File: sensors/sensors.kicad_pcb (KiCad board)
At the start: 2 copper layers, 20 x 50 mm, 6 parts, among them J1 Conn 1x3, U1 TCRT5000

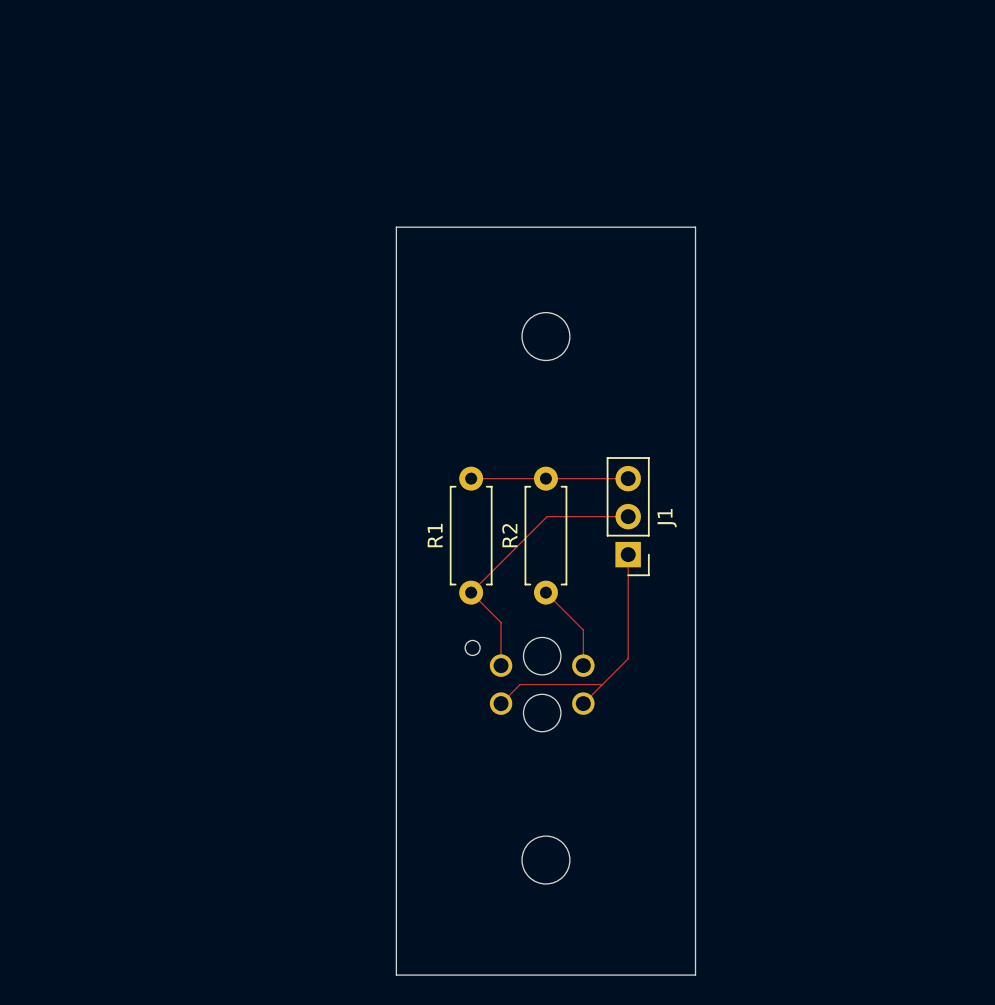
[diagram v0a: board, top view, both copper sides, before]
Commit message: Added a potentiometer to the sensor board.
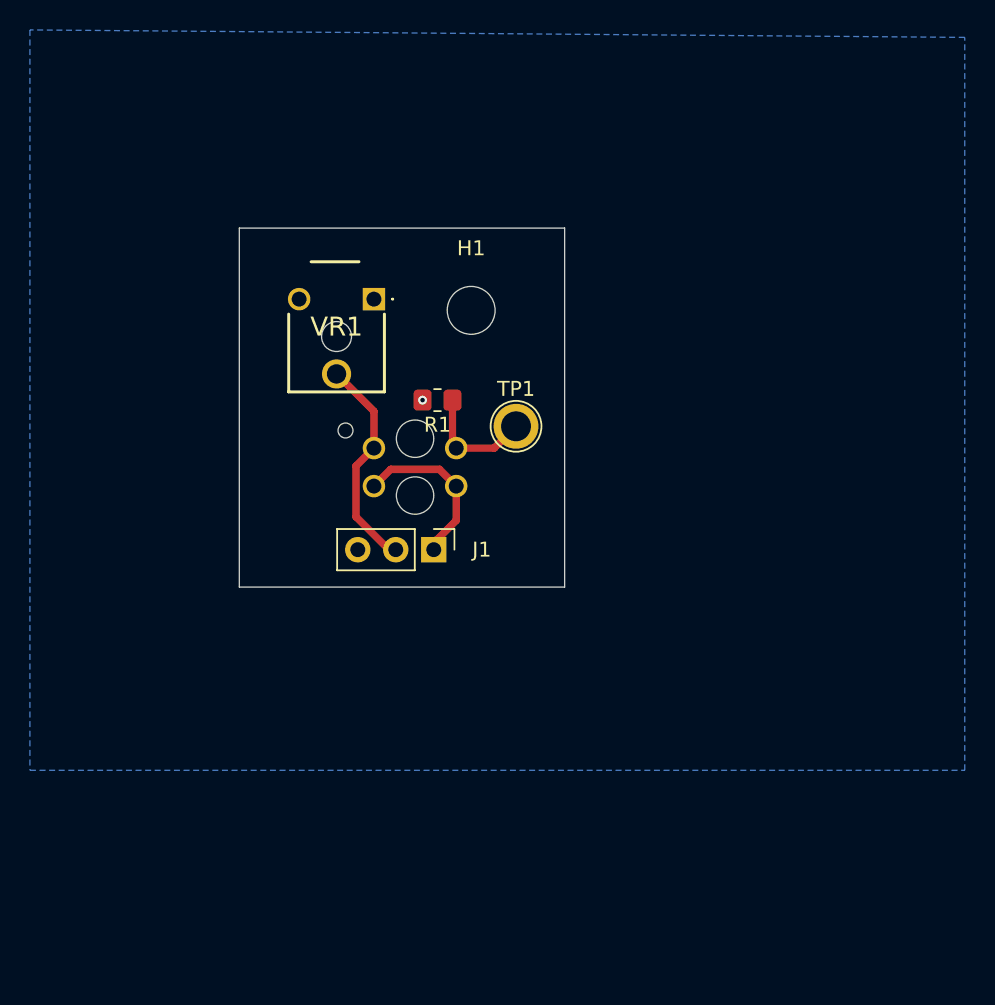
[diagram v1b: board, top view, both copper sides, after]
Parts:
- removed H2: MountingHole, MountingHole:MountingHole_3.2mm_M3
- removed R2: 2k, Resistor_THT:R_Axial_DIN0207_L6.3mm_D2.5mm_P7.62mm_Horizontal
- added TP1: Cathode, TestPoint:TestPoint_Plated_Hole_D2.0mm, F.Cu at (158.5, 75.5)
- added VR1: N6L50T0C-102-3030, N6L50T0C-103-3030:N6L50T0C1033030, F.Cu at (149.0, 67.0)
- R1: value 50R -> 2k2; footprint Resistor_THT:R_Axial_DIN0207_L6.3mm_D2.5mm_P7.62mm_Horizontal -> Resistor_SMD:R_0805_2012Metric_Pad1.20x1.40mm_HandSolder
- moved U1 16.8 mm to (151.8, 78.2)
- moved R1 13.1 mm to (153.2, 73.8), turned to 180 degrees
- moved J1 13.0 mm to (153.0, 83.8), turned to -90 degrees
- moved H1 5.30 mm to (155.5, 67.8)
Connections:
- net Vss renamed Vcc
- R1 pad 1: Vout -> Net-(R1-Pad1)
- U1 pad 4: Net-(R2-Pad1) -> Net-(R1-Pad1)
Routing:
- net GND: track 10.5 -> 0.00 mm, vias 0 -> 1
- net Net-(R1-Pad1): track 0.00 -> 7.97 mm
- net Vcc: track 18.5 -> 11.5 mm
- net Net-(R2-Pad1): track 5.92 -> 0.00 mm
- net Vout: track 18.3 -> 14.2 mm
- added copper zone on B.Cu, net GND
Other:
- board size 20 x 50 mm -> 21.8 x 24 mm
